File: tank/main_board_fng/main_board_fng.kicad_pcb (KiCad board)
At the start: 2 copper layers, 71.5 x 61.5 mm, 46 parts, among them J11 M0, J12 M1, J13 M2, U1 L7805, U2 ATMEGA328P-PU, U3 SN74HC595, U4 TB6612FNG, U5 TB6612FNG, Y1 Crystal

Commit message: FNG WIP
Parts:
- removed J12: M1, Connector_JST:JST_EH_B2B-EH-A_1x02_P2.50mm_Vertical
- added J1: M1, Connector_JST:JST_EH_B2B-EH-A_1x02_P2.50mm_Vertical, F.Cu at (159.5, 98.0)
- moved J11 13.8 mm to (159.5, 88.5)
- moved C5 11.2 mm to (101.1, 117.9), turned to 180 degrees
- moved C1 9.09 mm to (122.5, 128.0), turned to 90 degrees
- moved C12 8.51 mm to (153.0, 100.5), turned to -90 degrees
- moved C14 7.40 mm to (146.0, 82.8), turned to -90 degrees
- moved U4 5.24 mm to (145.5, 92.6)
- moved C15 5.23 mm to (152.0, 84.0)
- moved PowerMotor1 4.75 mm to (159.7, 107.8)
- moved J13 4.50 mm to (159.5, 117.5)
- moved C8 4.46 mm to (136.0, 102.3), turned to 0 degrees
- moved C3 4.10 mm to (125.0, 115.0), turned to -90 degrees
- moved C9 3.15 mm to (134.8, 119.5)
- moved C11 2.55 mm to (135.9, 109.8)
- moved C10 2.53 mm to (136.1, 95.8)
- moved U5 2.50 mm to (145.5, 114.0)
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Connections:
- C11 pad 2: Net-(U5-STBY) -> 4.5V
- C12 pad 2: Net-(U5-VM1) -> Vm
- C13 pad 2: Net-(U5-VM1) -> Vm
- C9 pad 2: Net-(U5-STBY) -> 4.5V
- U5 pad 13: Net-(U5-VM1) -> Vm
- U5 pad 14: Net-(U5-VM1) -> Vm
- U5 pad 19: Net-(U5-STBY) -> 4.5V
- U5 pad 20: Net-(U5-STBY) -> 4.5V
- U5 pad 24: Net-(U5-VM1) -> Vm
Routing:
- net GND: track 0.00 -> 399.3 mm, vias 0 -> 2
- net 4.5V: track 0.00 -> 281.1 mm, vias 0 -> 3
- net Gm: track 0.00 -> 94.0 mm
- net Vm: track 0.00 -> 86.5 mm
- net LED0: track 0.00 -> 79.4 mm
- net LED2: track 0.00 -> 68.1 mm
- net M1PWM: track 0.00 -> 67.0 mm, vias 0 -> 2
- net LED1: track 0.00 -> 66.1 mm
- net Net-(U2-(PCINT14/~{RESET})PC6): track 0.00 -> 59.0 mm
- net M0PWM: track 0.00 -> 54.9 mm
- net IRRx: track 0.00 -> 44.9 mm
- net SERIAL_DATA: track 0.00 -> 44.5 mm
- net Encoder1: track 0.00 -> 44.3 mm
- net M2+: track 0.00 -> 39.0 mm
- net Net-(U2-(PCINT23/AIN1)PD7): track 0.00 -> 36.8 mm
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- added copper zone on B.Cu, net Gm

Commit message: main board v0.14
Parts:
- removed J1: M1, Connector_JST:JST_EH_B2B-EH-A_1x02_P2.50mm_Vertical
- removed J11: M0, Connector_JST:JST_EH_B2B-EH-A_1x02_P2.50mm_Vertical
- removed J13: M2, Connector_JST:JST_EH_B2B-EH-A_1x02_P2.50mm_Vertical
- added G***: LOGO, custom:Tank, B.Cu at (145.3, 122.6)
- added M0: M0, TerminalBlock_Phoenix:TerminalBlock_Phoenix_MKDS-1,5-2_1x02_P5.00mm_Horizontal, F.Cu at (158.3, 100.2)
- added M1: M1, TerminalBlock_Phoenix:TerminalBlock_Phoenix_MKDS-1,5-2_1x02_P5.00mm_Horizontal, F.Cu at (158.3, 88.8)
- added M2: M2, TerminalBlock_Phoenix:TerminalBlock_Phoenix_MKDS-1,5-2_1x02_P5.00mm_Horizontal, F.Cu at (158.3, 124.5)
- PowerMotor1: footprint Connector_JST:JST_EH_B2B-EH-A_1x02_P2.50mm_Vertical -> TerminalBlock_Phoenix:TerminalBlock_Phoenix_MKDS-1,5-2_1x02_P5.00mm_Horizontal
- moved C14 16.8 mm to (144.5, 99.5)
- moved C15 16.0 mm to (150.4, 99.9)
- moved C8 14.5 mm to (140.2, 88.5), turned to 180 degrees
- moved C9 13.8 mm to (140.5, 107.0), turned to 180 degrees
- moved C12 9.86 mm to (144.5, 105.5)
- moved U5 6.44 mm to (147.7, 120.1), turned to 180 degrees
- moved C11 5.33 mm to (140.5, 112.5), turned to 180 degrees
- moved C10 4.34 mm to (140.0, 94.0), turned to 180 degrees
- moved PowerMotor1 4.30 mm to (158.4, 111.8)
- moved NT1 4.01 mm to (143.8, 128.5), turned to 180 degrees
- moved C13 3.74 mm to (150.6, 106.4)
- moved U4 1.88 mm to (147.4, 92.6), turned to 180 degrees
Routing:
- net Gm: track 94.0 -> 70.3 mm, vias 0 -> 122
- net Vm: track 86.5 -> 67.1 mm
- net Net-(J11-Pin_1): track 25.3 -> 10.2 mm
- net Net-(J13-Pin_1): track 20.3 -> 7.62 mm
- net Net-(J11-Pin_2): track 20.3 -> 10.2 mm
- net Net-(J13-Pin_2): track 17.1 -> 7.34 mm
- net M0PWM: track 54.9 -> 46.9 mm
- net Net-(J1-Pin_1): track 15.1 -> 8.64 mm
- net M1PWM: track 67.0 -> 61.0 mm, vias 2 -> 0
- net M0-: track 26.6 -> 22.0 mm, vias 1 -> 0
- net M2+: track 39.0 -> 34.6 mm
- net M0+: track 18.0 -> 13.6 mm, vias 1 -> 0
- net 4.5V: track 281.1 -> 284.9 mm, vias 3 -> 4
- net M1-: track 27.4 -> 31.1 mm
- net M2PWM: track 34.4 -> 36.8 mm
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- added copper zone on F.Cu, net Gm
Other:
- board text added: "Laser Tag Robot Tank Main Board v0.14 M.I.A.R. Labs nick.groesz@gmail.com"

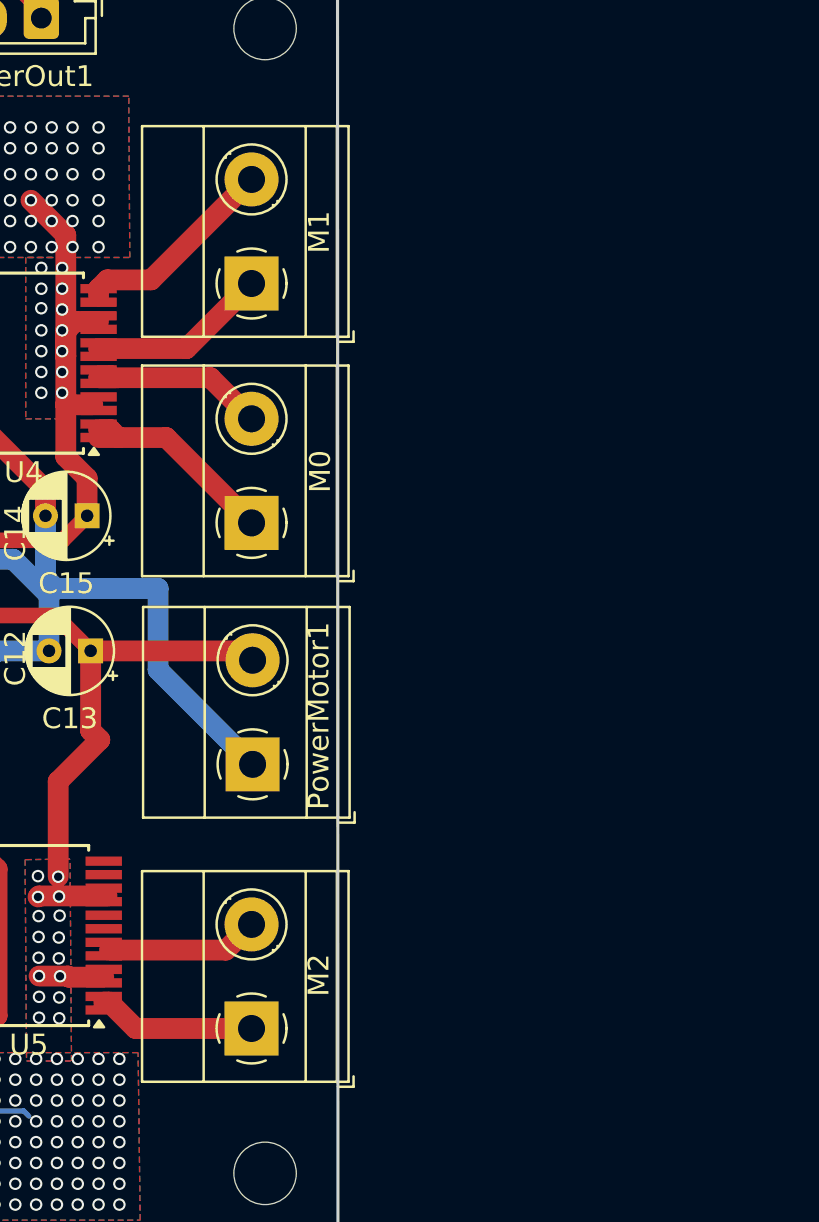
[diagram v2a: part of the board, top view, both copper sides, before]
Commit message: Main Board v0.15
Changes:
    - back to L293 motor driver
    - add speaker resistor
    - 3.5mm pitch screw terminals for motors and motor power
    - move programming header
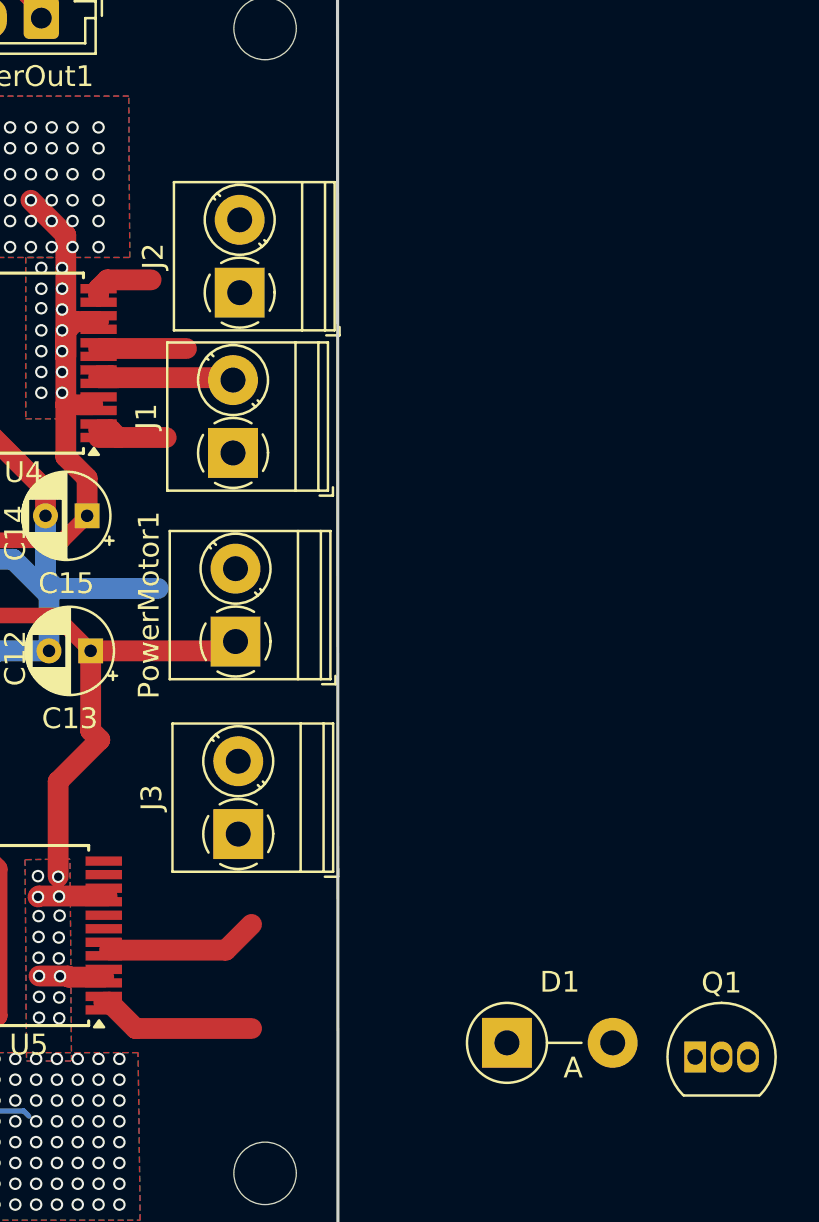
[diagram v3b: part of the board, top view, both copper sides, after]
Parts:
- removed M0: M0, TerminalBlock_Phoenix:TerminalBlock_Phoenix_MKDS-1,5-2_1x02_P5.00mm_Horizontal
- removed M1: M1, TerminalBlock_Phoenix:TerminalBlock_Phoenix_MKDS-1,5-2_1x02_P5.00mm_Horizontal
- removed M2: M2, TerminalBlock_Phoenix:TerminalBlock_Phoenix_MKDS-1,5-2_1x02_P5.00mm_Horizontal
- added D1: 1N4148, Diode_THT:D_DO-15_P5.08mm_Vertical_AnodeUp, F.Cu at (170.6, 125.2)
- added J1: M0, TerminalBlock_Phoenix:TerminalBlock_Phoenix_PT-1,5-2-3.5-H_1x02_P3.50mm_Horizontal, F.Cu at (157.5, 96.9)
- added J2: M1, TerminalBlock_Phoenix:TerminalBlock_Phoenix_PT-1,5-2-3.5-H_1x02_P3.50mm_Horizontal, F.Cu at (157.8, 89.2)
- added J3: M2, TerminalBlock_Phoenix:TerminalBlock_Phoenix_PT-1,5-2-3.5-H_1x02_P3.50mm_Horizontal, F.Cu at (157.7, 115.2)
- added Q1: 2N3904, Package_TO_SOT_THT:TO-92_Inline, F.Cu at (179.7, 125.9)
- PowerMotor1: footprint TerminalBlock_Phoenix:TerminalBlock_Phoenix_MKDS-1,5-2_1x02_P5.00mm_Horizontal -> TerminalBlock_Phoenix:TerminalBlock_Phoenix_PT-1,5-2-3.5-H_1x02_P3.50mm_Horizontal
- moved PowerMotor1 5.96 mm to (157.6, 106.0)
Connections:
- U4 pad 19: 4.5V -> Net-(Q1-E)
- U5 pad 19: 4.5V -> Net-(Q1-E)
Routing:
- net Vm: track 67.1 -> 56.8 mm
- net Net-(J2-Pin_2): track 9.90 -> 3.08 mm
- net Net-(J1-Pin_1): track 10.2 -> 4.36 mm
- net Net-(J2-Pin_1): track 8.64 -> 4.22 mm
- net Net-(J1-Pin_2): track 10.2 -> 7.42 mm
- net Gm: track 70.3 -> 69.7 mm
